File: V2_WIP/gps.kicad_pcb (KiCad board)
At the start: 6 copper layers, 82.5 x 82.5 mm, 132 parts, among them J301 USB_B_Micro, J601 BATT, P1 USB_C_Plug_USB2.0, Q1 IRLML5203, Q2 S8050, Q3 S8050, SW1 RotaryEncoder, SW3 SW_Push, SW4 SW_Push, SW601 MSN22AFW01, U1 ESP32-WROOM-32E, U10 24C32, U11 SN74LV1T34DBVRG4, U12 RT9742AGJ5F, U13 TP4057, U14 CH340K, U2 TPS613222ADBVR, U301 USBLC6-2SC6, U4 HT16k33, U401 NEO-M9N, U402 KW4-804CGB, U5 7seg_1x1_rgb, U6 7seg_1x1_rgb, U601 IP5306, U602 STC3100IST, U7 7seg_1x1_rgb, U9 TCA39306DDFR

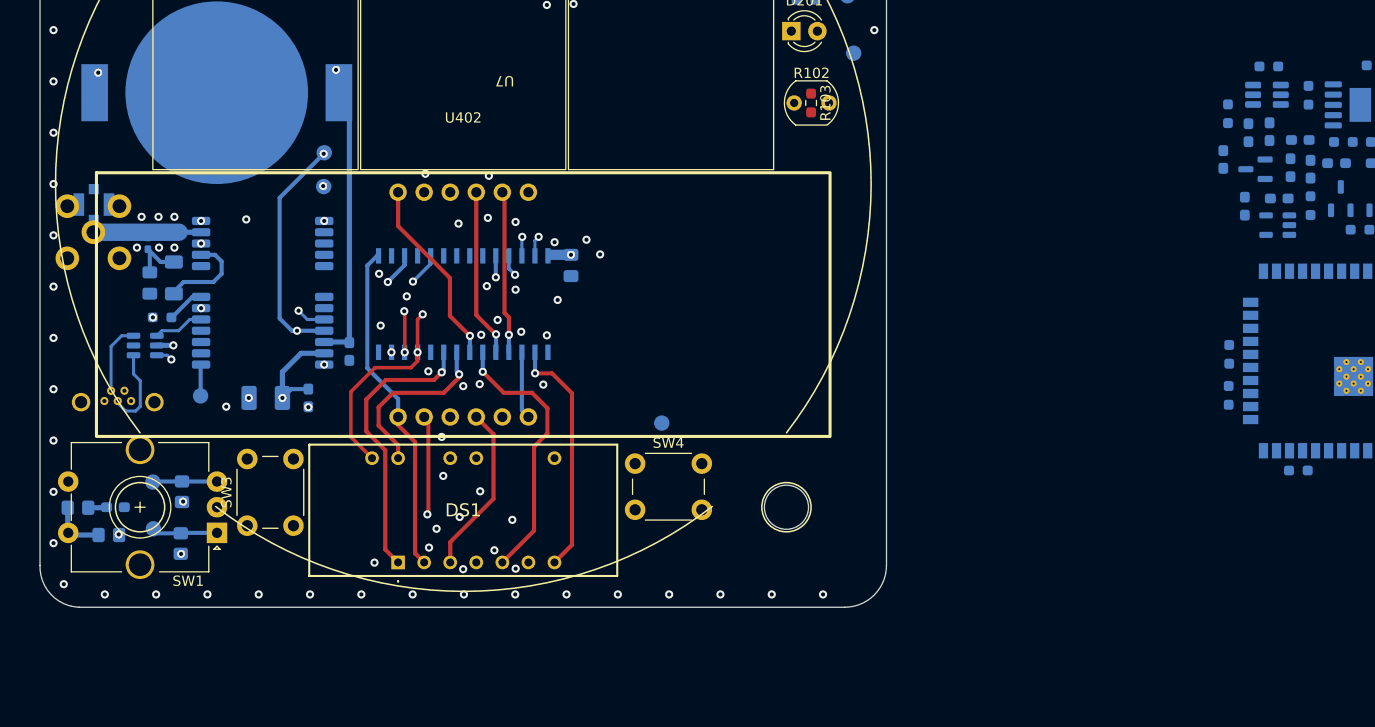
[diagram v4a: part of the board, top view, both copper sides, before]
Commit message: added FLASH module; moved encoder into separate schematic
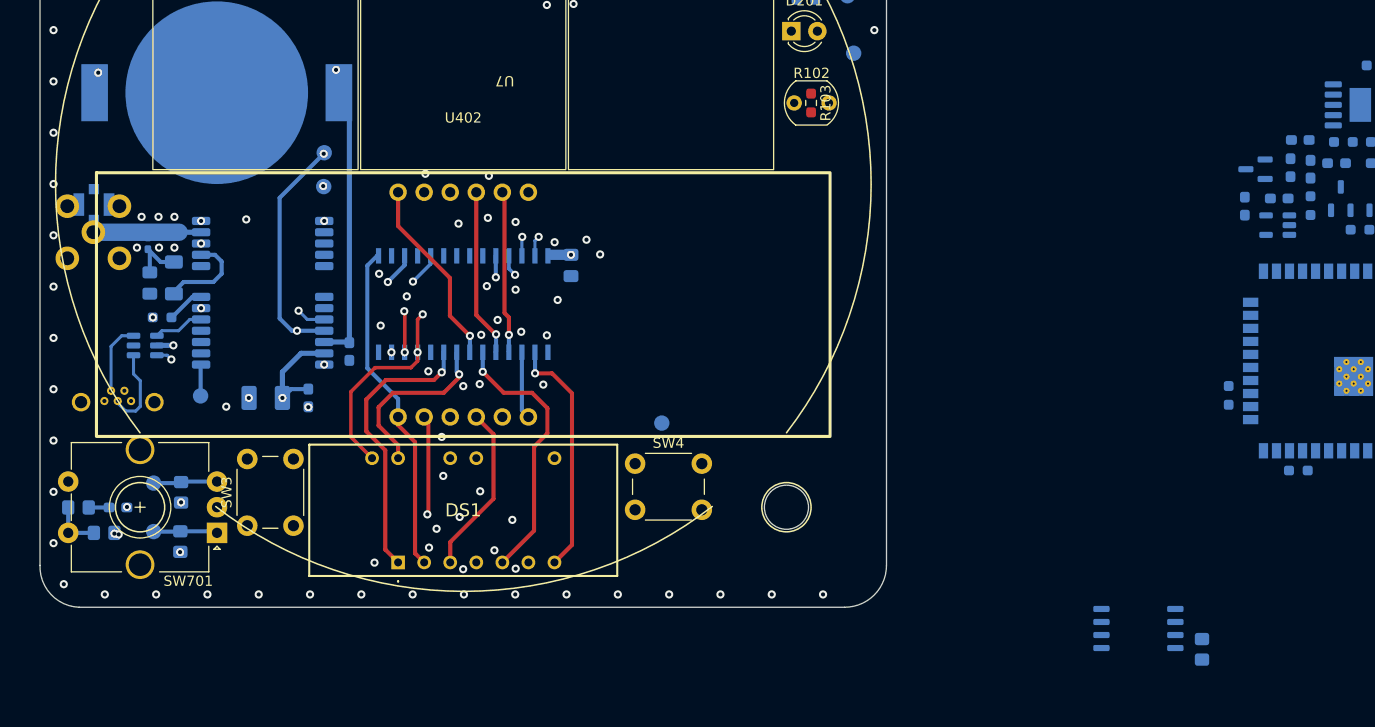
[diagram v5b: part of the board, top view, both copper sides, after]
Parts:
- removed C101: 100n, Capacitor_SMD:C_0603_1608Metric_Pad1.08x0.95mm_HandSolder
- removed C12, C13: 10u, Capacitor_SMD:C_0603_1608Metric_Pad1.08x0.95mm_HandSolder
- removed D5: LED, Diode_SMD:D_0603_1608Metric_Pad1.05x0.95mm_HandSolder
- removed R104: 0R, Resistor_SMD:R_0603_1608Metric_Pad0.98x0.95mm_HandSolder
- removed R13, R14: 2k, Resistor_SMD:R_0603_1608Metric_Pad0.98x0.95mm_HandSolder
- removed R201: 0.1, Resistor_SMD:R_0603_1608Metric_Pad0.98x0.95mm_HandSolder
- removed R_E1, R_E2, R_E3: 10k, Resistor_SMD:R_0805_2012Metric_Pad1.20x1.40mm_HandSolder
- removed R_E101: 1k, Resistor_SMD:R_0805_2012Metric_Pad1.20x1.40mm_HandSolder
- removed SW1: RotaryEncoder, Rotary_Encoder:RotaryEncoder_Alps_EC12E-Switch_Vertical_H20mm_CircularMountingHoles
- removed TP4: DT, TestPoint:TestPoint_Pad_D1.5mm
- removed TP9: CLK, TestPoint:TestPoint_Pad_D1.5mm
- removed U13: TP4057, Package_TO_SOT_SMD:SOT-23-6_Handsoldering
- added C701: 100n, Capacitor_SMD:C_0603_1608Metric_Pad1.08x0.95mm_HandSolder, B.Cu at (60.4, 114.5)
- added R_E102: 10k, Resistor_SMD:R_0805_2012Metric_Pad1.20x1.40mm_HandSolder, B.Cu at (166.0, 128.3)
- added R_E701: 10k, Resistor_SMD:R_0805_2012Metric_Pad1.20x1.40mm_HandSolder, B.Cu at (59.0, 117.0)
- added R_E702: 10k, Resistor_SMD:R_0805_2012Metric_Pad1.20x1.40mm_HandSolder, B.Cu at (66.4, 117.8)
- added R_E703: 1k, Resistor_SMD:R_0805_2012Metric_Pad1.20x1.40mm_HandSolder, B.Cu at (56.5, 114.5)
- added R_E704: 10k, Resistor_SMD:R_0805_2012Metric_Pad1.20x1.40mm_HandSolder, B.Cu at (66.5, 113.0)
- added SW701: RotaryEncoder, Rotary_Encoder:RotaryEncoder_Alps_EC12E-Switch_Vertical_H20mm_CircularMountingHoles, F.Cu at (70.0, 117.0)
- added TP701: CLK, TestPoint:TestPoint_Pad_D1.5mm, B.Cu at (63.8, 116.9)
- added TP702: DT, TestPoint:TestPoint_Pad_D1.5mm, B.Cu at (63.8, 112.2)
- added U102: W25Q128JFV, Package_SO:SOIC-8_5.23x5.23mm_P1.27mm, B.Cu at (159.8, 126.3)
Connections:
- U1 pad 26: /ESP/IO4/D12 -> /CS_N
- U1 pad 30: /ESP/IO18/SCK -> /SCK
- U1 pad 31: /ESP/IO19/MISO -> /MISO
- U1 pad 37: /ESP/IO23/MOSI -> /MOSI
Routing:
- net Net-(R_E101-Pad1): track 5.52 -> 0.00 mm
- net Net-(R_E701-Pad1): track 0.00 -> 5.34 mm
- net GND: vias 115 -> 116
- net +3V3: vias 6 -> 7
